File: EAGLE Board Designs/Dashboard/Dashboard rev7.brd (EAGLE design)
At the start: 247.6 x 47.4 mm, 121 parts, among them J1 CONNECTOR-4_μF_S_RA_, J10 CONNECTOR-10__, J2 CONNECTOR-8_μF_S_RA_, J3 CONNECTOR-4_μF_S_RA_, J4 CONNECTOR-6_μF_S_RA_, J5 CONNECTOR-10__, J6 CONNECTOR-6_μF_S_RA_, J7 CONNECTOR-4_538-505110-0492_, J8 USB4110, J9 CONNECTOR-4_538-505110-0492_, U1 NEOPIXEL_IN-PI55QATPRPGPBPW-40, U10 NEOPIXEL_IN-PI55QATPRPGPBPW-40, U12 NEOPIXEL_IN-PI55QATPRPGPBPW-40, U13 NEOPIXEL_IN-PI55QATPRPGPBPW-40, U14 NEOPIXEL_IN-PI55QATPRPGPBPW-40, U15 NEOPIXEL_IN-PI55QATPRPGPBPW-40, U16 STM32-LQFP64, U17 VOLTAGE_REGULATOR_SOT-223_3.3V, U2 NEOPIXEL_IN-PI55QATPRPGPBPW-40, U27 TCAN1051HQV-Q1, U3 MCP23S08, U4 NEOPIXEL_IN-PI55QATPRPGPBPW-40, U5 RE46C100, U6 NEOPIXEL_IN-PI55QATPRPGPBPW-40, U7 NEOPIXEL_IN-PI55QATPRPGPBPW-40, U8 NEOPIXEL_IN-PI55QATPRPGPBPW-40, U9 NEOPIXEL_IN-PI55QATPRPGPBPW-40, X1 24_MHZ_XTAL_OSCILLATOR

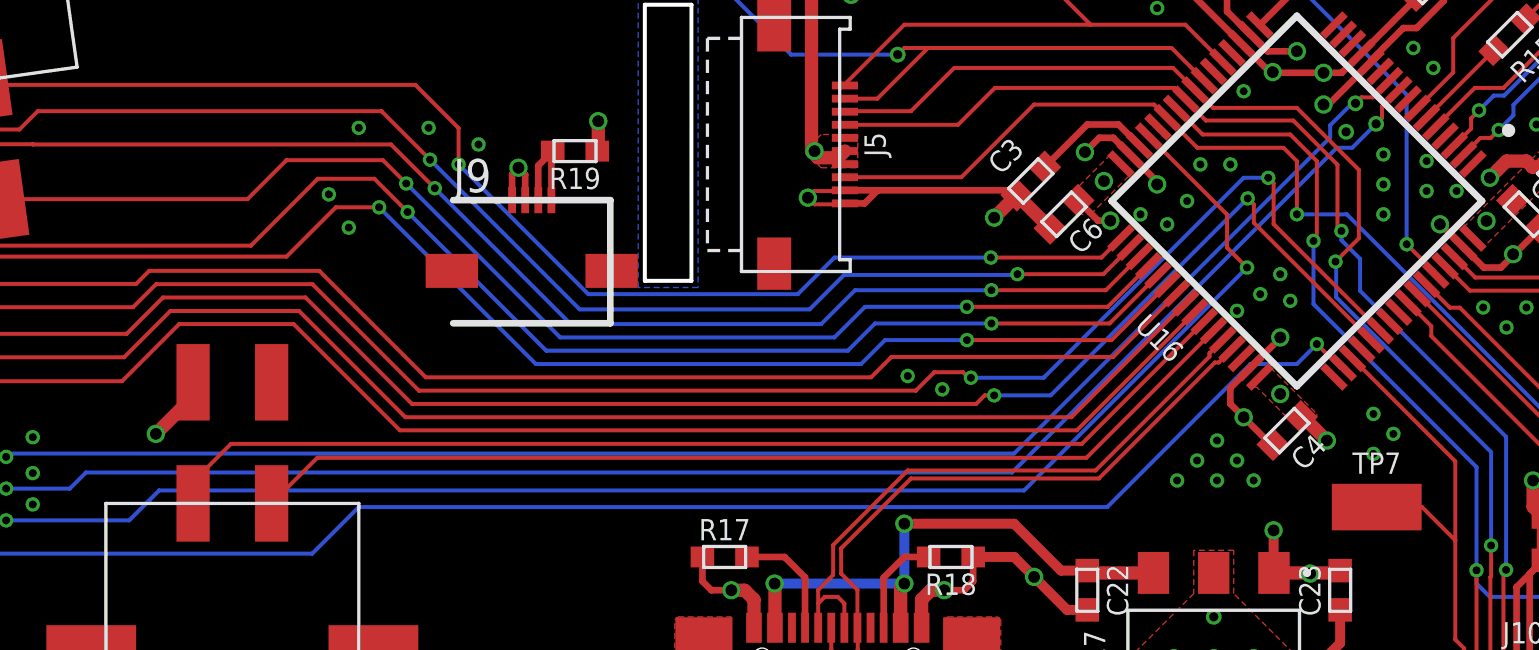
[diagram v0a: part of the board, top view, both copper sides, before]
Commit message: Cleanup, better GND return path for SPI2
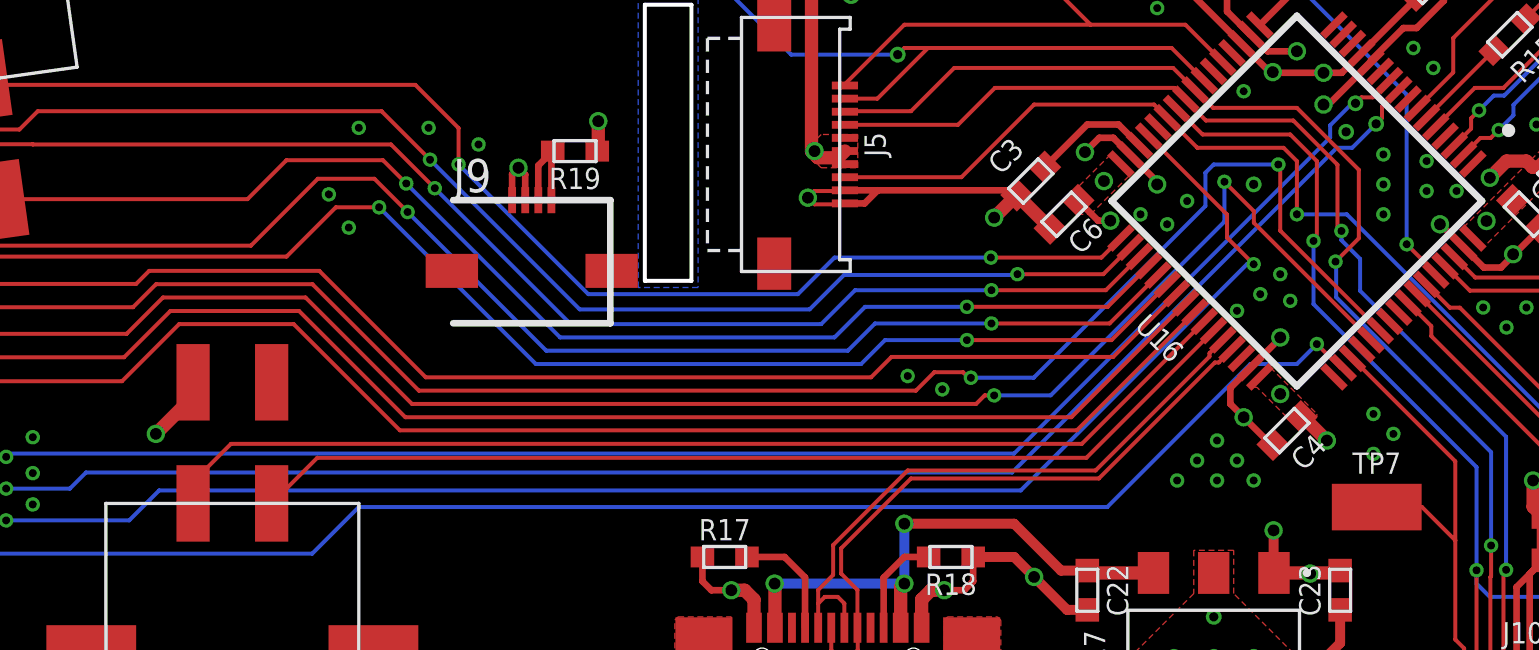
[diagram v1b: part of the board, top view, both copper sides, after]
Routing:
- net BTN_MODE_READ: track 86.5 -> 88.2 mm
- net BTN_START_READ: track 88.6 -> 89.9 mm
- net GND: vias 129 -> 128
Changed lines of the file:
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@@
 <via x="72.263" y="-52.578" extent="1-16" drill="0.3"/>
 <via x="70.485" y="-53.086" extent="1-16" drill="0.3"/>
-<via x="72.771" y="-51.181" extent="1-16" drill="0.3"/>
-<via x="73.914" y="-51.181" extent="1-16" drill="0.3"/>
 <via x="79.756" y="-50.8" extent="1-16" drill="0.3"/>
 <via x="79.756" y="-51.943" extent="1-16" drill="0.3"/>
@@
 <via x="73.406" y="-63.246" extent="1-16" drill="0.3"/>
 <via x="71.882" y="-63.246" extent="1-16" drill="0.3"/>
+<via x="74.803" y="-51.943" extent="1-16" drill="0.35"/>
 </signal>
 <signal name="+12V">
@@
 <wire x1="64.008" y1="-59.3245125" x2="63.9210625" y2="-59.3245125" width="0.1524" layer="1"/>
 <wire x1="63.9210625" y1="-59.3245125" x2="63.71053125" y2="-59.11398125" width="0.1524" layer="1"/>
-<wire x1="79.635978125" y1="-57.527746875" x2="75.565" y2="-53.45676875" width="0.1524" layer="1"/>
-<wire x1="75.565" y1="-51.8943875" x2="75.36240625" y2="-51.69179375" width="0.1524" layer="1"/>
-<via x="75.36240625" y="-51.69179375" extent="1-16" drill="0.3"/>
-<wire x1="75.565" y1="-53.45676875" x2="75.565" y2="-51.8943875" width="0.1524" layer="1"/>
-<wire x1="75.36240625" y1="-51.69179375" x2="74.41920625" y2="-51.69179375" width="0.1524" layer="16"/>
-<wire x1="66.7864875" y1="-59.3245125" x2="64.008" y2="-59.3245125" width="0.1524" layer="16"/>
-<wire x1="74.41920625" y1="-51.69179375" x2="66.7864875" y2="-59.3245125" width="0.1524" layer="16"/>
+<wire x1="79.635978125" y1="-57.527746875" x2="75.819" y2="-53.71076875" width="0.1524" layer="1"/>
+<via x="75.74340625" y="-51.18379375" extent="1-16" drill="0.3"/>
+<wire x1="75.74340625" y1="-51.18379375" x2="75.819" y2="-51.2593875" width="0.1524" layer="1"/>
+<wire x1="75.819" y1="-51.2593875" x2="75.819" y2="-53.71076875" width="0.1524" layer="1"/>
+<wire x1="66.4054875" y1="-59.3245125" x2="64.008" y2="-59.3245125" width="0.1524" layer="16"/>
+<wire x1="66.4054875" y1="-59.3245125" x2="72.9615" y2="-52.7685" width="0.1524" layer="16"/>
 <wire x1="63.71053125" y1="-59.11398125" x2="62.611" y2="-59.11398125" width="0.1524" layer="1"/>
 <wire x1="62.611" y1="-59.11398125" x2="61.90798125" y2="-59.817" width="0.1524" layer="1"/>
 <wire x1="61.90798125" y1="-59.817" x2="42.9350375" y2="-59.817" width="0.1524" layer="1"/>
 <wire x1="42.9350375" y1="-59.817" x2="38.87103125" y2="-55.75299375" width="0.1524" layer="1"/>
+<wire x1="72.9615" y1="-52.7685" x2="72.9615" y2="-51.4985" width="0.1524" layer="16"/>
+<wire x1="72.9615" y1="-51.4985" x2="73.27620625" y2="-51.18379375" width="0.1524" layer="16"/>
+<wire x1="73.27620625" y1="-51.18379375" x2="75.74340625" y2="-51.18379375" width="0.1524" layer="16"/>
 </signal>
 <signal name="BTN_MC_CYCLE_READ">
@@
 <via x="64.897" y="-59.9976" extent="1-16" drill="0.3"/>
 <wire x1="79.282425" y1="-57.8813" x2="74.81100625" y2="-53.40988125" width="0.1524" layer="1"/>
-<wire x1="74.81100625" y1="-52.71300625" x2="74.5761" y2="-52.4781" width="0.1524" layer="1"/>
-<via x="74.5761" y="-52.4781" extent="1-16" drill="0.3"/>
-<wire x1="74.81100625" y1="-53.40988125" x2="74.81100625" y2="-52.71300625" width="0.1524" layer="1"/>
+<wire x1="74.81100625" y1="-52.96700625" x2="73.6871" y2="-51.8431" width="0.1524" layer="1"/>
+<via x="73.6871" y="-51.8431" extent="1-16" drill="0.3"/>
+<wire x1="74.81100625" y1="-53.40988125" x2="74.81100625" y2="-52.96700625" width="0.1524" layer="1"/>
 <wire x1="64.897" y1="-59.9976" x2="67.056" y2="-59.9976" width="0.1524" layer="16"/>
-<wire x1="74.5755" y1="-52.4781" x2="74.5761" y2="-52.4781" width="0.1524" layer="16"/>
-<wire x1="67.056" y1="-59.9976" x2="74.5755" y2="-52.4781" width="0.1524" layer="16"/>
+<wire x1="73.6871" y1="-53.3665" x2="73.6871" y2="-51.8431" width="0.1524" layer="16"/>
+<wire x1="67.056" y1="-59.9976" x2="73.6871" y2="-53.3665" width="0.1524" layer="16"/>
 </signal>
 <signal name="BOTS">
@@
 <via x="27.178" y="-64.77" extent="1-16" drill="0.3"/>
 <wire x1="70.79714375" y1="-50.103125" x2="73.787" y2="-53.09298125" width="0.1524" layer="1"/>
-<wire x1="73.787" y1="-53.09298125" x2="73.787" y2="-54.356" width="0.1524" layer="1"/>
-<wire x1="73.787" y1="-54.356" x2="74.549" y2="-55.118" width="0.1524" layer="1"/>
-<via x="74.549" y="-55.118" extent="1-16" drill="0.3"/>
-<wire x1="74.549" y1="-55.118" x2="66.04" y2="-63.627" width="0.1524" layer="16"/>
+<wire x1="73.787" y1="-53.09298125" x2="73.787" y2="-53.975" width="0.1524" layer="1"/>
+<wire x1="73.787" y1="-53.975" x2="74.803" y2="-54.991" width="0.1524" layer="1"/>
+<via x="74.803" y="-54.991" extent="1-16" drill="0.3"/>
+<wire x1="74.803" y1="-54.991" x2="74.549" y2="-54.991" width="0.1524" layer="16"/>
+<wire x1="74.549" y1="-54.991" x2="65.913" y2="-63.627" width="0.1524" layer="16"/>
 <wire x1="33.02" y1="-63.627" x2="31.877" y2="-64.77" width="0.1524" layer="16"/>
 <wire x1="31.877" y1="-64.77" x2="27.178" y2="-64.77" width="0.1524" layer="16"/>
-<wire x1="66.04" y1="-63.627" x2="33.02" y2="-63.627" width="0.1524" layer="16"/>
+<wire x1="65.913" y1="-63.627" x2="33.02" y2="-63.627" width="0.1524" layer="16"/>
 </signal>
 <signal name="MCU_SPI3_MOSI">

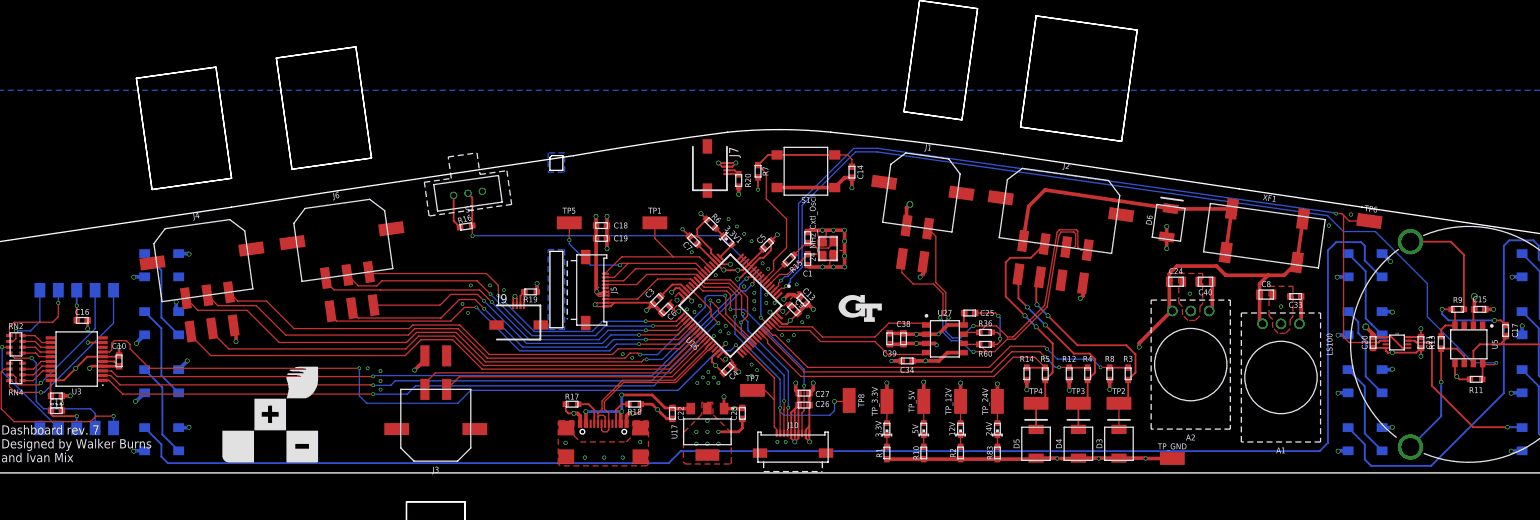
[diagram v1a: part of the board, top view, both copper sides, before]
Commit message: Finishing touches, silkscreen modification, changed dial connector, added decoupling cap
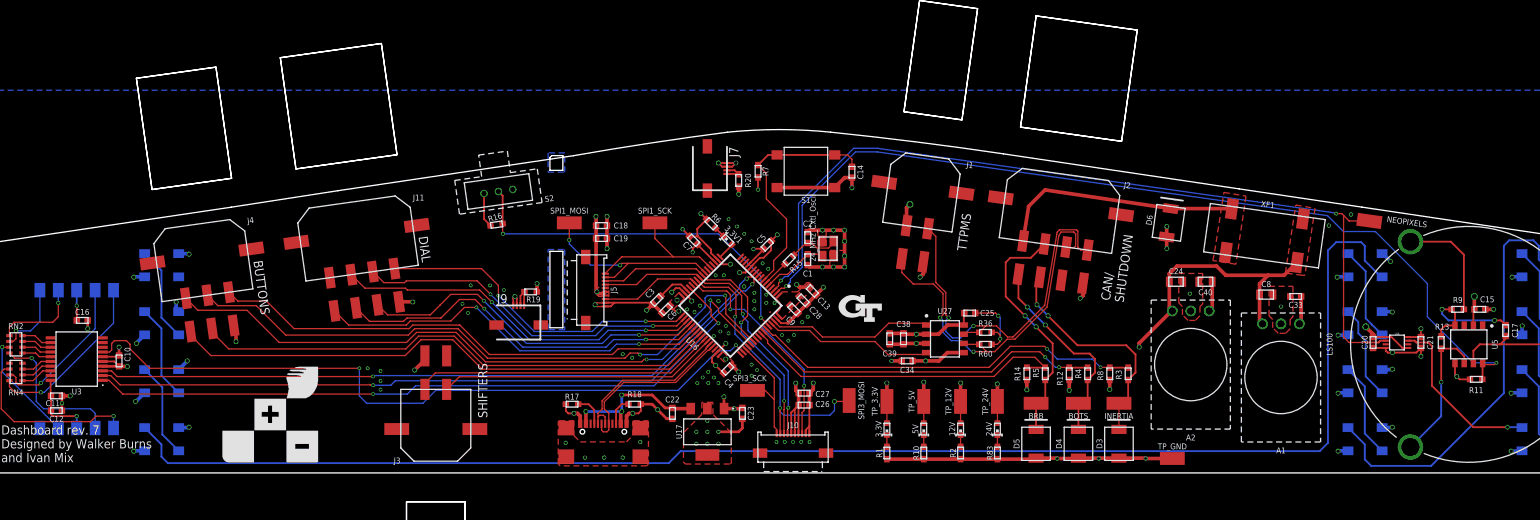
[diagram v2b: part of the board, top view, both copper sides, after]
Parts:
- removed J6: CONNECTOR-6_μF_S_RA_, HyTechDevices:MOLEX_MICROFIT_SMD_RIGHTANGLE_06_DUAL
- added C28: CAPACITOR_0603_10V_0.1UF, HyTechDevices:0603-CAP
- added J11: CONNECTOR-8_μF_S_RA_, HyTechDevices:MOLEX_MICROFIT_SMD_RIGHTANGLE_08_DUAL
- moved S2 4.20 mm to (44.5, -36.8)
- moved R16 4.20 mm to (44.2, -41.4)
- moved C13 1.80 mm to (87.8, -50.5)
- renumbered TP1 to SPI1_SCK, TP2 to INERTIA, TP3 to BOTS, TP4 to BRB, TP5 to SPI1_MOSI, TP6 to NEOPIXELS, TP7 to SPI3_SCK, TP8 to SPI3_MOSI
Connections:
- removed net VBAT: U16.P$1
- net +3V3: now also C28.1, U16.P$1
- net DIAL_AUTOCROSS: now also J11.5; no longer J6.4
- net DIAL_ENDURANCE: now also J11.4; no longer J6.3
- net DIAL_LAUNCH: now also J11.7; no longer J6.6
- net DIAL_MODE_1: now also J11.3; no longer J6.2
- net DIAL_MODE_2: now also J11.2; no longer J6.1
- net DIAL_SKIDPAD: now also J11.6; no longer J6.5
- net GND: now also C28.2, J11.8
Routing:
- net +3V3: track 212.4 -> 196.7 mm, vias 19 -> 18
- net +5V: track 123.6 -> 109.6 mm, vias 30 -> 27
- net 24VIN: track 40.1 -> 34.0 mm
- net +24V: track 72.0 -> 66.0 mm
- net MCU_BOOT_0: track 55.5 -> 51.4 mm
- net DIAL_MODE_1: track 51.5 -> 47.8 mm
- net DIAL_MODE_2: track 54.7 -> 51.1 mm
- net GND: track 238.1 -> 234.7 mm, vias 128 -> 126
- net DIAL_ENDURANCE: track 48.2 -> 44.9 mm
- net DIAL_LAUNCH: track 48.1 -> 48.7 mm
- added copper zone on layer 1, net +24V
- added copper zone on layer 1, net 24VIN
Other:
- board text added: "BUTTONS"
- board text added: "CAN/ SHUTDOWN"
- board text added: "DIAL"
- board text added: "SHIFTERS"
- board text added: "TTPMS"

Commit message: Added jumper and shottky for bypassing VBUS capacitance
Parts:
- added D1: SCHOTTKY_SOD323_30VV, HyTechDevices:SOD-323
- added U$12: JUMPER_3PIN, HyTechDevices:1X03
- moved U$7 4.95 mm to (92.5, -57.5)
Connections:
- new net 5V_IN: A1.3, C33.1, D1.A, U$12.1
- new net DISP_5V: C18.1, C19.1, C26.1, C27.1, J10.7, J10.8, J10.9, J5.7, J5.8, J5.9, J7.1, J7.2, J9.1, J9.2, U$12.2
- net +5V: now also D1.C, U$12.3; no longer A1.3, C18.1, C19.1, C26.1, C27.1, C33.1, J10.7, J10.8, J10.9, J5.7, J5.8, J5.9, J7.1, J7.2, J9.1, J9.2
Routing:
- net DISP_5V: track 0.00 -> 123.5 mm, vias 0 -> 3
- net 5V_IN: track 0.00 -> 77.1 mm
- net +5V: track 109.6 -> 70.3 mm, vias 27 -> 21
- net GND: vias 126 -> 194
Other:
- board text added: "BOOT"
- board text added: "FLASH"

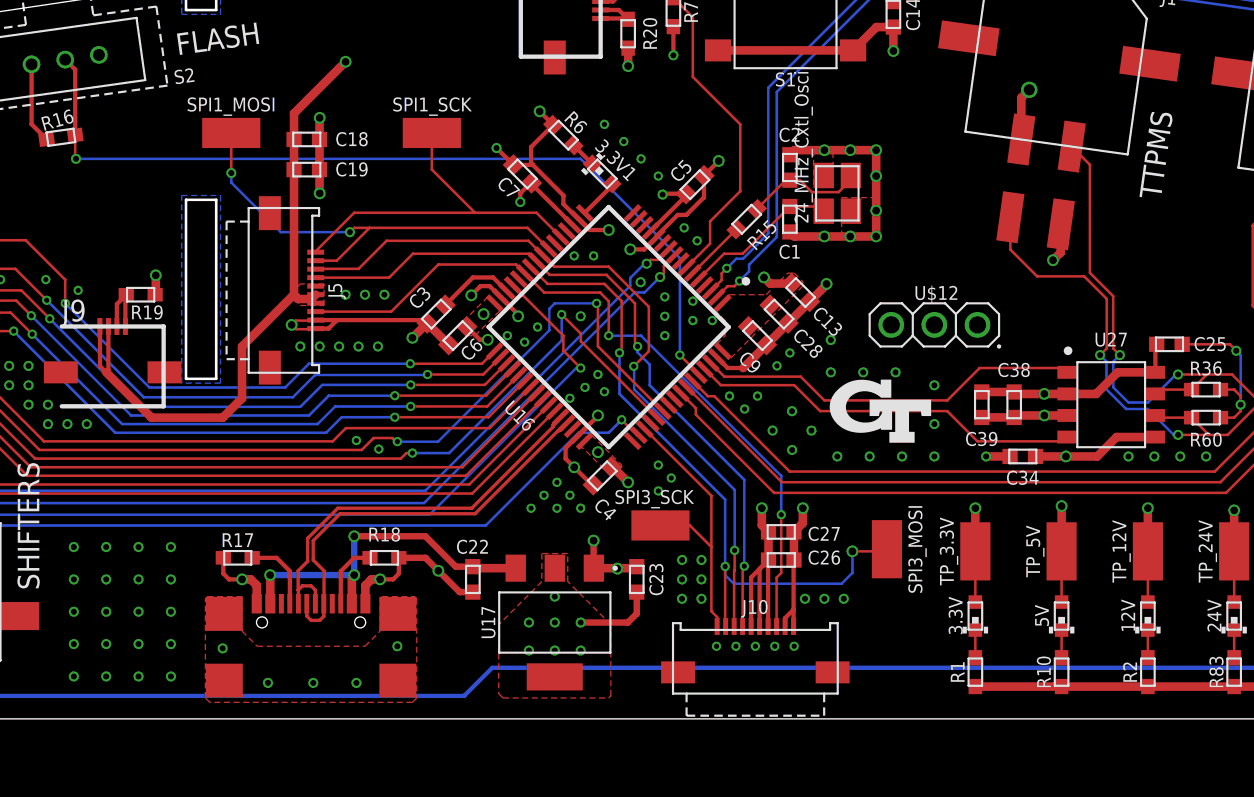
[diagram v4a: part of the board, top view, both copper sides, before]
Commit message: Changed LEDs and Resistor values
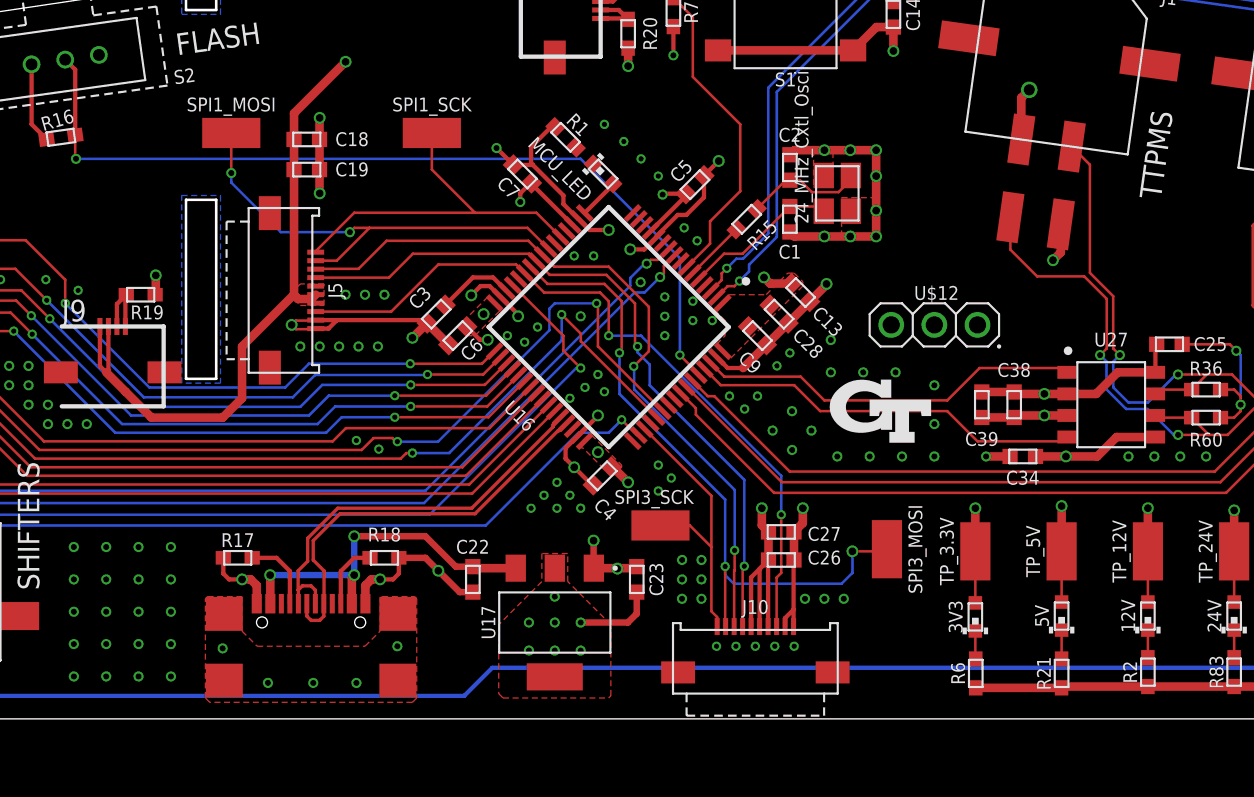
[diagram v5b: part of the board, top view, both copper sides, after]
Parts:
- removed 3.3V, 3.3V1: LED_0603_GREEN, HyTechDevices - Copy:0603-LED
- removed R10: RESISTOR_0603_1K, HyTechDevices:0603-RES
- added 3V3, MCU_LED: LED_0603_GREEN_2V2, HyTechDevices:0603-LED
- added R21: RESISTOR_0603_180, HyTechDevices:0603-RES
- R1, R6: value RESISTOR_0603_1K -> RESISTOR_0603_240
- moved R6 39.9 mm to (98.1, -73.0), turned to 90 degrees
- moved R1 39.7 mm to (73.9, -41.4), turned to 315 degrees
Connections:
- net +3V3: now also 3V3.2; no longer 3.3V.2
- net GND: now also R21.1; no longer R10.1
- net MCU_LED: now also MCU_LED.2; no longer 3.3V1.2
- net N$11: now also MCU_LED.1, R1.2; no longer 3.3V1.1, R6.2
- net N$31: now also 3V3.1, R6.2; no longer 3.3V.1, R1.2
- net N$32: now also R21.2; no longer R10.2
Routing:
- net N$11: track 1.56 -> 0.05 mm
- net GND: track 234.7 -> 233.6 mm, vias 194 -> 193

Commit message: Modifications/cleanup
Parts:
- removed D1: SCHOTTKY_SOD323_30VV, HyTechDevices:SOD-323
- added D2: SCHOTTKY__15V, HyTechDevices:DO-214BA
- C22, C29: value CAPACITOR_0603_25V_10UF -> CAPACITOR_0603_10V_4.7UF
- moved TP_GND 2.29 mm to (135.1, -73.7)
- moved C22 0.25 mm to (68.2, -67.4)
- renumbered C23 to C29
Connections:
- net +5V: now also D2.2; no longer D1.C
- net 5V_IN: now also D2.1; no longer D1.A
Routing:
- net +5V: track 70.3 -> 102.0 mm, vias 21 -> 25
- net 5V_IN: track 77.1 -> 105.3 mm
- net GND: track 233.6 -> 231.1 mm, vias 193 -> 247
- net N$11: track 0.05 -> 1.43 mm
- net MCU_NRST: track 34.4 -> 33.6 mm
- added copper zone on layer 1, net DISP_5V
- added copper zone on layer 16, net GND1
- added copper zone on layer 16, net GND2
- removed copper zone on layer 1, net +5V
